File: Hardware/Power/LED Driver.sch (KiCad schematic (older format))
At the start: 7 parts, among them IC2 BP1360

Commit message: Moved MCU Power Supply to Logic Board
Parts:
- D2: Arrow Part Number (none) -> C13763; Mouser Part Number C13763 -> (none)
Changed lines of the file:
@@
 F 2 "ArduinoLamp:D_SMC_Handsoldering_Shortened" H 6250 3900 50  0001 C CNN
 F 3 "~" H 6250 3900 50  0001 C CNN
-F 4 "C13763" H 6250 3900 50  0001 C CNN "Mouser Part Number"
+F 4 "" H 6250 3900 50  0001 C CNN "Mouser Part Number"
+F 5 "C13763" H 6250 3900 50  0001 C CNN "Arrow Part Number"
 	1    6250 3900
 	1    0    0    -1

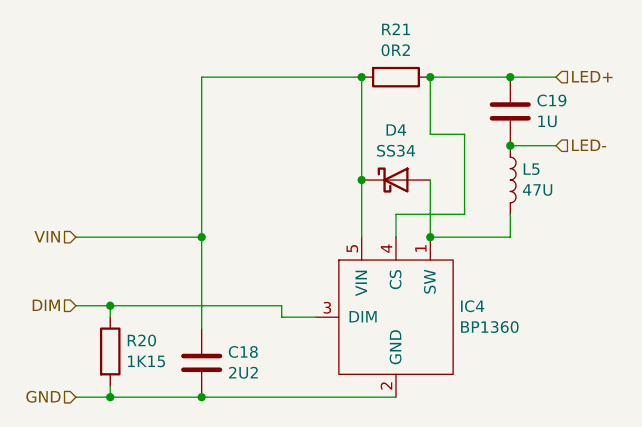
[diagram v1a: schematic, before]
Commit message: Removed Logic Board PSU from Power Board
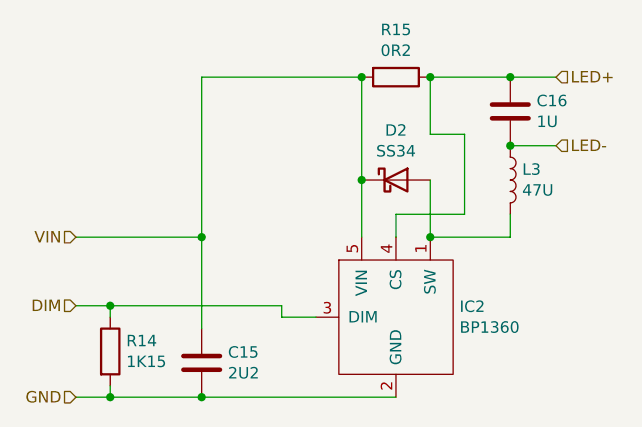
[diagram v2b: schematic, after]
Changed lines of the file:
@@
 $Descr A4 11693 8268
 encoding utf-8
-Sheet 4 7
+Sheet 3 7
 Title ""
 Date ""
@@
 AR Path="/5F8DDC00/5F8E3C51" Ref="C15"  Part="1"
 AR Path="/5F8D89C6/5F8E3C51" Ref="C18"  Part="1"
-F 0 "C18" H 5515 4746 50  0000 L CNN
+F 0 "C15" H 5515 4746 50  0000 L CNN
 F 1 "2U2" H 5515 4655 50  0000 L CNN
 F 2 "Capacitor_SMD:C_0805_2012Metric_Pad1.15x1.40mm_HandSolder" H 5438 4550 50  0001 C CNN
@@
 AR Path="/5F8DDC00/5F8E47BD" Ref="IC2"  Part="1"
 AR Path="/5F8D89C6/5F8E47BD" Ref="IC4"  Part="1"
-F 0 "IC4" H 6528 4346 50  0000 L CNN
+F 0 "IC2" H 6528 4346 50  0000 L CNN
 F 1 "BP1360" H 6528 4255 50  0000 L CNN
 F 2 "Package_TO_SOT_SMD:SOT-23-5_HandSoldering" H 5800 4750 50  0001 C CNN
@@
 AR Path="/5F8DDC00/5F8E5B58" Ref="R15"  Part="1"
 AR Path="/5F8D89C6/5F8E5B58" Ref="R21"  Part="1"
-F 0 "R21" V 6043 3450 50  0000 C CNN
+F 0 "R15" V 6043 3450 50  0000 C CNN
 F 1 "0R2" V 6134 3450 50  0000 C CNN
 F 2 "Resistor_SMD:R_1206_3216Metric_Pad1.42x1.75mm_HandSolder" V 6180 3450 50  0001 C CNN
@@
 AR Path="/5F8DDC00/5F8E74F3" Ref="D2"  Part="1"
 AR Path="/5F8D89C6/5F8E74F3" Ref="D4"  Part="1"
-F 0 "D4" H 6250 4117 50  0000 C CNN
+F 0 "D2" H 6250 4117 50  0000 C CNN
 F 1 "SS34" H 6250 4026 50  0000 C CNN
 F 2 "ArduinoLamp:D_SMC_Handsoldering_Shortened" H 6250 3900 50  0001 C CNN
@@
 AR Path="/5F8DDC00/5F8E819A" Ref="L3"  Part="1"
 AR Path="/5F8D89C6/5F8E819A" Ref="L5"  Part="1"
-F 0 "L5" H 6802 3946 50  0000 L CNN
+F 0 "L3" H 6802 3946 50  0000 L CNN
 F 1 "47U" H 6802 3855 50  0000 L CNN
 F 2 "ArduinoLamp:SLD10" H 6750 3900 50  0001 C CNN
@@
 AR Path="/5F8DDC00/5F8E8A71" Ref="C16"  Part="1"
 AR Path="/5F8D89C6/5F8E8A71" Ref="C19"  Part="1"
-F 0 "C19" H 6865 3646 50  0000 L CNN
+F 0 "C16" H 6865 3646 50  0000 L CNN
 F 1 "1U" H 6865 3555 50  0000 L CNN
 F 2 "Capacitor_SMD:C_0805_2012Metric_Pad1.15x1.40mm_HandSolder" H 6788 3450 50  0001 C CNN
@@
 AR Path="/5F8DDC00/5F8EB4DA" Ref="R14"  Part="1"
 AR Path="/5F8D89C6/5F8EB4DA" Ref="R20"  Part="1"
-F 0 "R20" H 5070 4696 50  0000 L CNN
+F 0 "R14" H 5070 4696 50  0000 L CNN
 F 1 "1K15" H 5070 4605 50  0000 L CNN
 F 2 "Resistor_SMD:R_0603_1608Metric_Pad1.05x0.95mm_HandSolder" V 4930 4650 50  0001 C CNN

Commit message: Fixed Power Board Errata
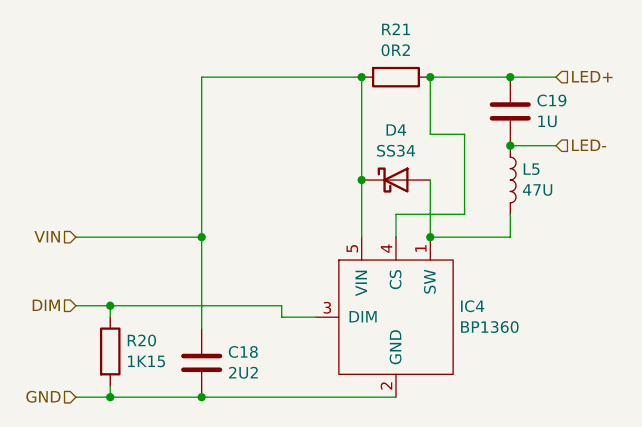
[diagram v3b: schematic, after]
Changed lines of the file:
@@
 AR Path="/5F8DDC00/5F8E3C51" Ref="C15"  Part="1"
 AR Path="/5F8D89C6/5F8E3C51" Ref="C18"  Part="1"
-F 0 "C15" H 5515 4746 50  0000 L CNN
+F 0 "C18" H 5515 4746 50  0000 L CNN
 F 1 "2U2" H 5515 4655 50  0000 L CNN
 F 2 "Capacitor_SMD:C_0805_2012Metric_Pad1.15x1.40mm_HandSolder" H 5438 4550 50  0001 C CNN
@@
 AR Path="/5F8DDC00/5F8E47BD" Ref="IC2"  Part="1"
 AR Path="/5F8D89C6/5F8E47BD" Ref="IC4"  Part="1"
-F 0 "IC2" H 6528 4346 50  0000 L CNN
+F 0 "IC4" H 6528 4346 50  0000 L CNN
 F 1 "BP1360" H 6528 4255 50  0000 L CNN
 F 2 "Package_TO_SOT_SMD:SOT-23-5_HandSoldering" H 5800 4750 50  0001 C CNN
@@
 AR Path="/5F8DDC00/5F8E5B58" Ref="R15"  Part="1"
 AR Path="/5F8D89C6/5F8E5B58" Ref="R21"  Part="1"
-F 0 "R15" V 6043 3450 50  0000 C CNN
+F 0 "R21" V 6043 3450 50  0000 C CNN
 F 1 "0R2" V 6134 3450 50  0000 C CNN
 F 2 "Resistor_SMD:R_1206_3216Metric_Pad1.42x1.75mm_HandSolder" V 6180 3450 50  0001 C CNN
@@
 AR Path="/5F8DDC00/5F8E74F3" Ref="D2"  Part="1"
 AR Path="/5F8D89C6/5F8E74F3" Ref="D4"  Part="1"
-F 0 "D2" H 6250 4117 50  0000 C CNN
+F 0 "D4" H 6250 4117 50  0000 C CNN
 F 1 "SS34" H 6250 4026 50  0000 C CNN
 F 2 "ArduinoLamp:D_SMC_Handsoldering_Shortened" H 6250 3900 50  0001 C CNN
@@
 AR Path="/5F8DDC00/5F8E819A" Ref="L3"  Part="1"
 AR Path="/5F8D89C6/5F8E819A" Ref="L5"  Part="1"
-F 0 "L3" H 6802 3946 50  0000 L CNN
+F 0 "L5" H 6802 3946 50  0000 L CNN
 F 1 "47U" H 6802 3855 50  0000 L CNN
 F 2 "ArduinoLamp:SLD10" H 6750 3900 50  0001 C CNN
@@
 AR Path="/5F8DDC00/5F8E8A71" Ref="C16"  Part="1"
 AR Path="/5F8D89C6/5F8E8A71" Ref="C19"  Part="1"
-F 0 "C16" H 6865 3646 50  0000 L CNN
+F 0 "C19" H 6865 3646 50  0000 L CNN
 F 1 "1U" H 6865 3555 50  0000 L CNN
 F 2 "Capacitor_SMD:C_0805_2012Metric_Pad1.15x1.40mm_HandSolder" H 6788 3450 50  0001 C CNN
@@
 AR Path="/5F8DDC00/5F8EB4DA" Ref="R14"  Part="1"
 AR Path="/5F8D89C6/5F8EB4DA" Ref="R20"  Part="1"
-F 0 "R14" H 5070 4696 50  0000 L CNN
+F 0 "R20" H 5070 4696 50  0000 L CNN
 F 1 "1K15" H 5070 4605 50  0000 L CNN
 F 2 "Resistor_SMD:R_0603_1608Metric_Pad1.05x0.95mm_HandSolder" V 4930 4650 50  0001 C CNN
